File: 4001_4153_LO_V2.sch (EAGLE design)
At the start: 108 parts, among them IC1 74LVC2G17GV,125, IC10 MCP6H01, IC2 74LVC2G17GV,125, IC3 74LVC2G17GV,125, IC4 ADF4001BRUZ, IC5 ATTINY45V-10SU, IC6 7805DT, IC7 7809DT, IC8 LD117ASTR, IC9 ADF4153BRUZ-RL7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

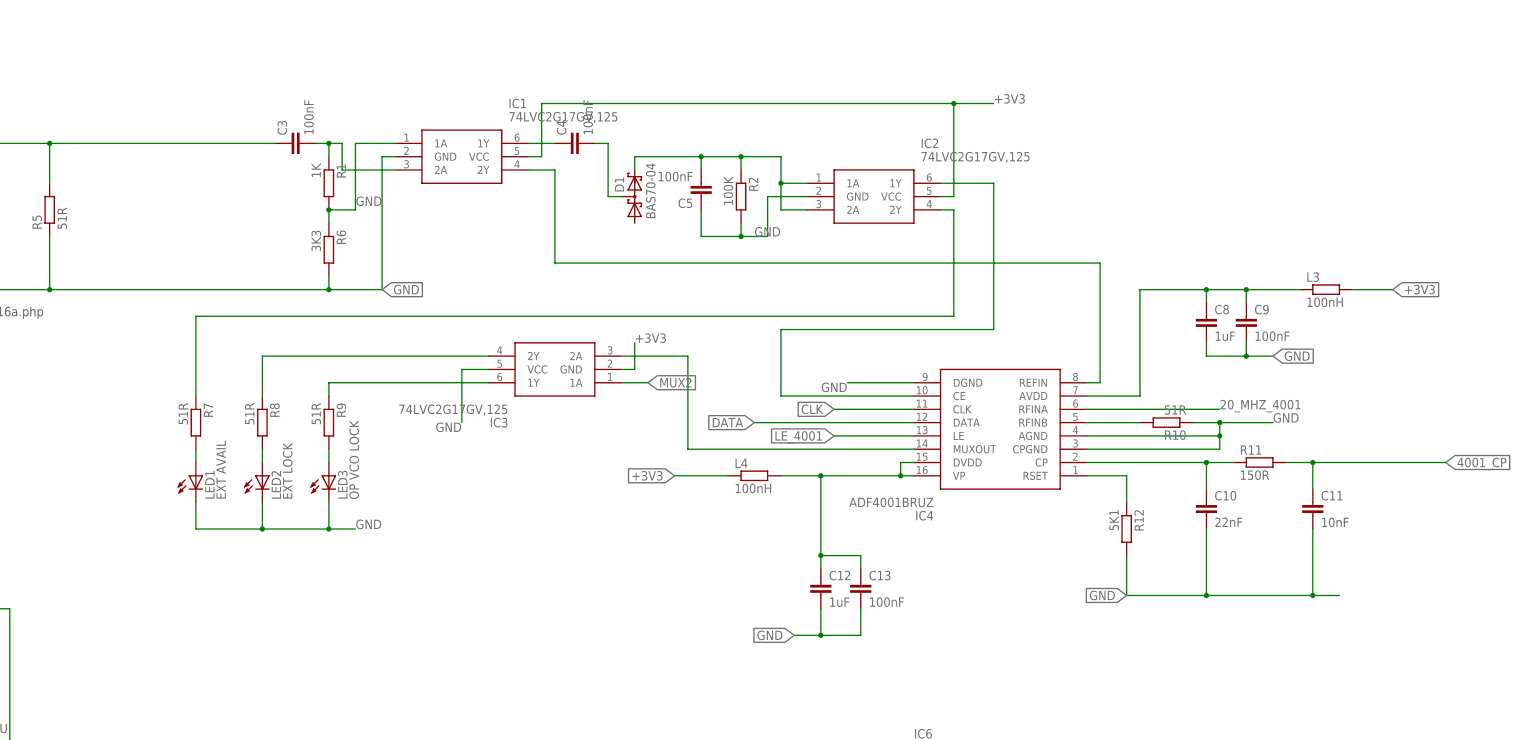
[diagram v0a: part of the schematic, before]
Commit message: Misc circuit revisions
Updated loop filter on 4001, added pullups to MUXOUT
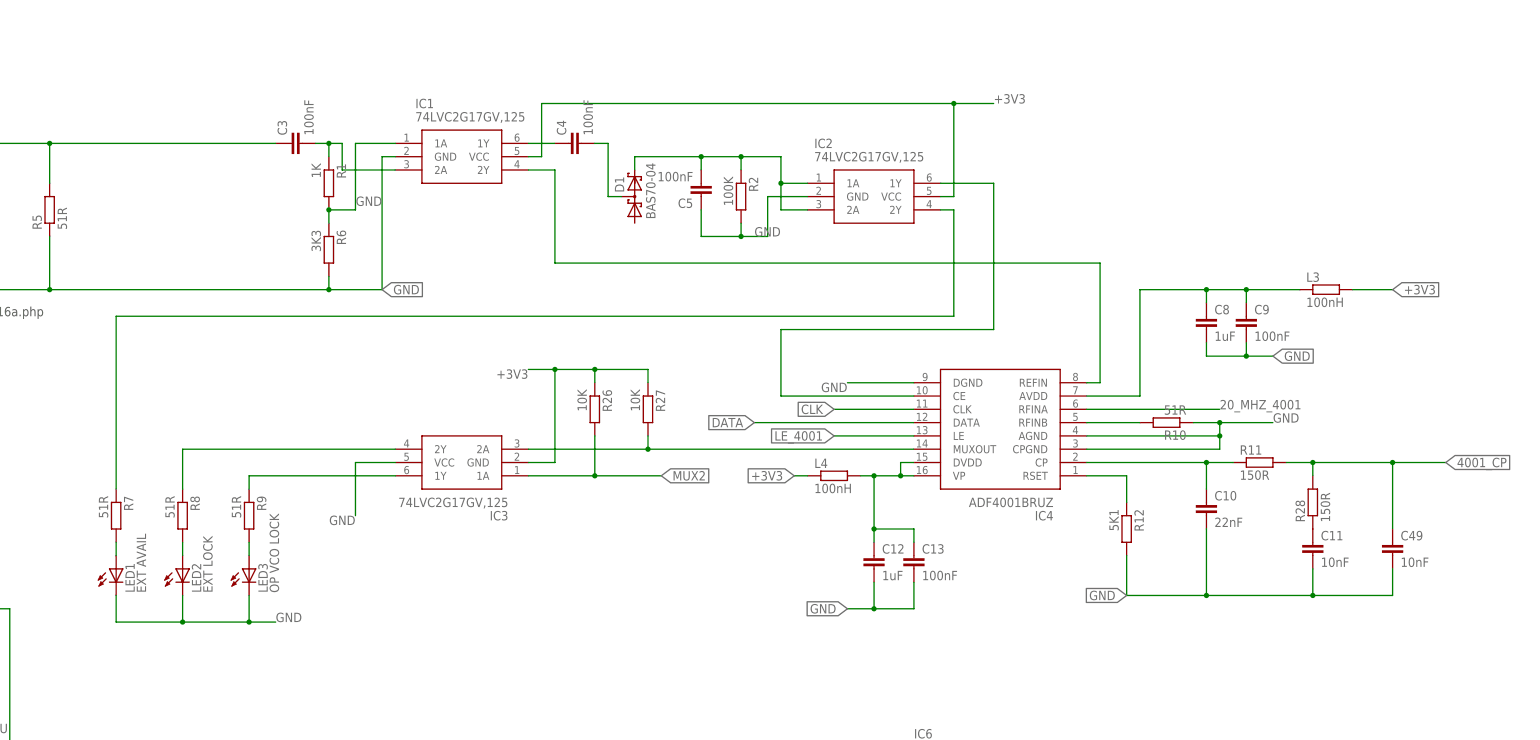
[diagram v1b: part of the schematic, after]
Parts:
- added C49: 10nF, resistor:C-EUC0603
- added R26, R27: 10K, rcl:R-EU_R0603
- added R28: 150R, rcl:R-EU_R0603
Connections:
- new net N$22: C11.1, R28.1
- net +3V3: now also R26.1, R27.1
- net 4001_CP: now also C49.1, R28.2; no longer C11.1
- net GND: now also C49.2
- net MUX2: now also R26.2
- net N$26: now also R27.2
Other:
- moved on the sheet: C11, C12, C13, IC3, L4, LED1, LED2, LED3, R7, R8, R9

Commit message: Output and detector
Moved resistor in output stage to power feed
Swapped C for R in 10MHz detector
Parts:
- removed C4: 100nF, resistor:C-EUC0603
- added R29: 100K, rcl:R-EU_R0603
- IC8: value LD117ASTR -> LD1117AS33TR
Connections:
- net N$11: now also C41.2; no longer R17.2
- net N$12: now also R17.1; no longer L7.1
- net N$21: now also L7.1, R17.2; no longer C41.2, R17.1
- net N$23: now also R29.2; no longer C4.2
- net N$30: now also R29.1; no longer C4.1
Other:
- moved on the sheet: L7, R17
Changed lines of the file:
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@@
 <part name="C21" library="rcl" deviceset="C-EU" device="C0805" value="100nF"/>
 <part name="VR1" library="resistor" deviceset="R-TRIMM" device="4G/J" value="1K"/>
-<part name="IC8" library="v-reg" deviceset="LD117A?*" device="S" technology="TR">
+<part name="IC8" library="v-reg" deviceset="LD117A?*" device="S" technology="TR" value="LD1117AS33TR">
 <attribute name="JLC" value="C108495"/>
 </part>
@@
 <part name="C3" library="resistor" deviceset="C-EU" device="C0603" value="100nF"/>
 <part name="D1" library="diode" deviceset="BAS70-04" device=""/>
-<part name="C4" library="resistor" deviceset="C-EU" device="C0603" value="100nF"/>
 <part name="C5" library="resistor" deviceset="C-EU" device="C0603" value="100nF"/>
 <part name="R2" library="rcl" deviceset="R-EU_" device="R0603" value="100K"/>
@@
 <part name="C49" library="resistor" deviceset="C-EU" device="C0603" value="10nF"/>
 <part name="R28" library="rcl" deviceset="R-EU_" device="R0603" value="150R"/>
+<part name="R29" library="rcl" deviceset="R-EU_" device="R0603" value="100K"/>
 </parts>
 <sheets>
@@
 <instance part="C31" gate="G$1" x="441.96" y="129.54"/>
 <instance part="C30" gate="G$1" x="434.34" y="129.54"/>
-<instance part="L7" gate="G$1" x="457.2" y="121.92" rot="R90"/>
+<instance part="L7" gate="G$1" x="457.2" y="129.54" rot="R90"/>
 <instance part="C38" gate="G$1" x="472.44" y="111.76" rot="R90"/>
 <instance part="R15" gate="G$1" x="403.86" y="114.3" rot="R270"/>
@@
 <instance part="C3" gate="G$1" x="299.72" y="345.44" rot="R90"/>
 <instance part="D1" gate="G$1" x="365.76" y="335.28" rot="R90"/>
-<instance part="C4" gate="G$1" x="353.06" y="345.44" rot="R90"/>
 <instance part="C5" gate="G$1" x="378.46" y="335.28" rot="R180"/>
 <instance part="R2" gate="G$1" x="386.08" y="335.28" rot="R270"/>
@@
 <instance part="C18" gate="G$1" x="454.66" y="223.52"/>
 <instance part="LSP1" gate="1" x="368.3" y="210.82"/>
-<instance part="R17" gate="G$1" x="436.88" y="106.68"/>
+<instance part="R17" gate="G$1" x="457.2" y="116.84" rot="R90"/>
 <instance part="R26" gate="G$1" x="358.14" y="294.64" rot="R270"/>
 <instance part="R27" gate="G$1" x="368.3" y="294.64" rot="R270"/>
 <instance part="C49" gate="G$1" x="510.54" y="269.24"/>
 <instance part="R28" gate="G$1" x="495.3" y="276.86" rot="R90"/>
+<instance part="R29" gate="G$1" x="355.6" y="345.44"/>
 </instances>
 <busses>
@@
 </segment>
 </net>
-<net name="N$11" class="0">
-<segment>
-<pinref part="Q1" gate="G$1" pin="G"/>
-<pinref part="R17" gate="G$1" pin="2"/>
-<wire x1="441.96" y1="106.68" x2="452.12" y2="106.68" width="0.1524" layer="91"/>
-</segment>
-</net>
 <net name="N$12" class="0">
 <segment>
 <pinref part="Q1" gate="G$1" pin="S"/>
 <wire x1="457.2" y1="109.22" x2="457.2" y2="111.76" width="0.1524" layer="91"/>
-<pinref part="L7" gate="G$1" pin="1"/>
 <pinref part="C38" gate="G$1" pin="1"/>
-<wire x1="457.2" y1="111.76" x2="457.2" y2="116.84" width="0.1524" layer="91"/>
 <wire x1="469.9" y1="111.76" x2="457.2" y2="111.76" width="0.1524" layer="91"/>
 <junction x="457.2" y="111.76"/>
+<pinref part="R17" gate="G$1" pin="1"/>
 </segment>
 </net>
@@
 <segment>
 <pinref part="L7" gate="G$1" pin="2"/>
-<wire x1="457.2" y1="127" x2="457.2" y2="137.16" width="0.1524" layer="91"/>
+<wire x1="457.2" y1="134.62" x2="457.2" y2="137.16" width="0.1524" layer="91"/>
 <pinref part="C30" gate="G$1" pin="1"/>
 <wire x1="457.2" y1="137.16" x2="441.96" y2="137.16" width="0.1524" layer="91"/>
@@
 <net name="N$23" class="0">
 <segment>
-<pinref part="C4" gate="G$1" pin="2"/>
-<wire x1="358.14" y1="345.44" x2="360.68" y2="345.44" width="0.1524" layer="91"/>
 <wire x1="360.68" y1="345.44" x2="360.68" y2="335.28" width="0.1524" layer="91"/>
 <pinref part="D1" gate="G$1" pin="C1A2"/>
 <wire x1="360.68" y1="335.28" x2="363.22" y2="335.28" width="0.1524" layer="91"/>
+<pinref part="R29" gate="G$1" pin="2"/>
 </segment>
 </net>
@@
 <segment>
 <pinref part="IC1" gate="G$1" pin="1Y"/>
-<pinref part="C4" gate="G$1" pin="1"/>
 <wire x1="345.44" y1="345.44" x2="350.52" y2="345.44" width="0.1524" layer="91"/>
+<pinref part="R29" gate="G$1" pin="1"/>
 </segment>
 </net>
@@
 </segment>
 </net>
-<net name="N$21" class="0">
-<segment>
-<pinref part="R17" gate="G$1" pin="1"/>
-<wire x1="424.18" y1="106.68" x2="431.8" y2="106.68" width="0.1524" layer="91"/>
-<pinref part="C41" gate="G$1" pin="2"/>
-</segment>
-</net>
 <net name="N$22" class="0">
 <segment>
@@
 </segment>
 </net>
+<net name="N$11" class="0">
+<segment>
+<pinref part="C41" gate="G$1" pin="2"/>
+<pinref part="Q1" gate="G$1" pin="G"/>
+<wire x1="424.18" y1="106.68" x2="452.12" y2="106.68" width="0.1524" layer="91"/>
+</segment>
+</net>
+<net name="N$21" class="0">
+<segment>
+<pinref part="L7" gate="G$1" pin="1"/>
+<wire x1="457.2" y1="121.92" x2="457.2" y2="124.46" width="0.1524" layer="91"/>
+<pinref part="R17" gate="G$1" pin="2"/>
+</segment>
+</net>

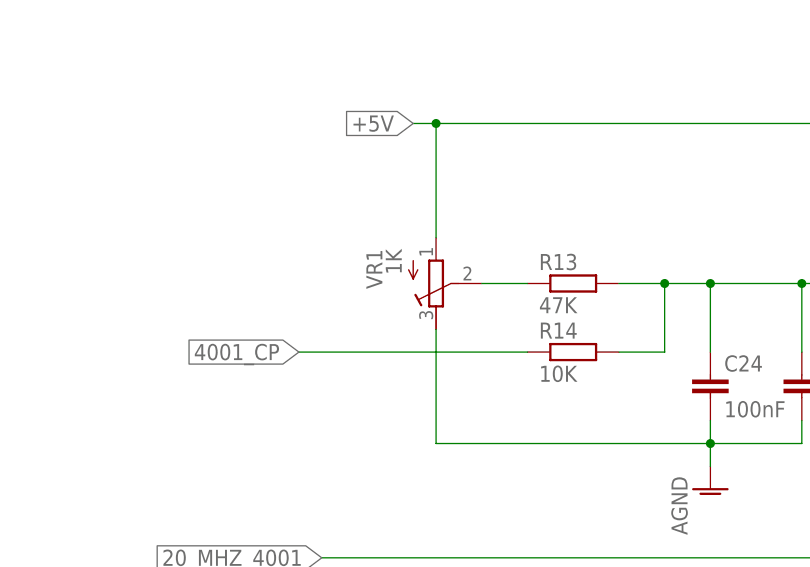
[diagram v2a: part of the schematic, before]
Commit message: multi-turn
replaced single turn pot with multiturn
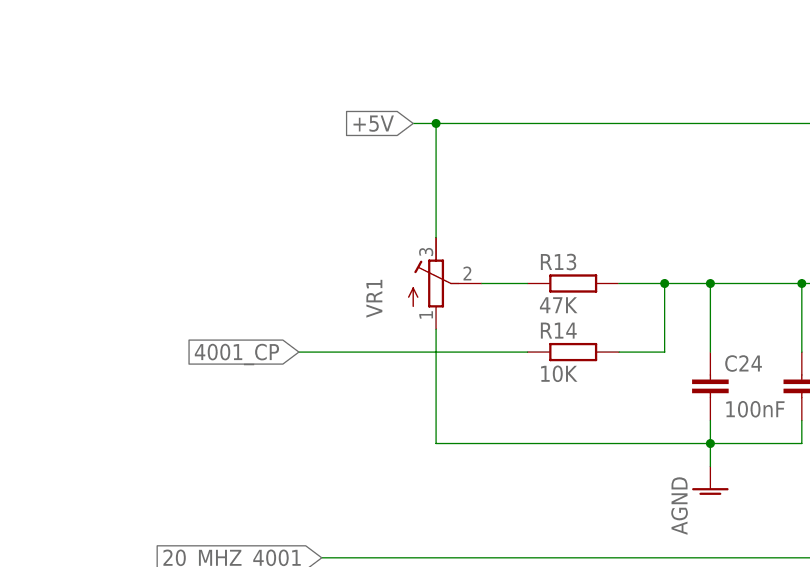
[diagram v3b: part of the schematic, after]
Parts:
- VR1: value 1K -> (none); device resistor:R-TRIMM4G/J -> resistor:R-TRIMM64Y
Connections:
- net +5V: now also VR1.A; no longer VR1.E
- net GND: now also VR1.E; no longer VR1.A
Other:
- moved on the sheet: VR1
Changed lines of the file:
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@@
 <part name="C20" library="rcl" deviceset="C-EU" device="C0805" value="10uF"/>
 <part name="C21" library="rcl" deviceset="C-EU" device="C0805" value="100nF"/>
-<part name="VR1" library="resistor" deviceset="R-TRIMM" device="4G/J" value="1K"/>
 <part name="IC8" library="v-reg" deviceset="LD117A?*" device="S" technology="TR" value="LD1117AS33TR">
 <attribute name="JLC" value="C108495"/>
@@
 <part name="R28" library="rcl" deviceset="R-EU_" device="R0603" value="150R"/>
 <part name="R29" library="rcl" deviceset="R-EU_" device="R0603" value="100K"/>
+<part name="VR1" library="resistor" deviceset="R-TRIMM" device="64Y"/>
 </parts>
 <sheets>
@@
 <instance part="C24" gate="G$1" x="147.32" y="165.1"/>
 <instance part="AGND40" gate="VR1" x="147.32" y="152.4"/>
-<instance part="VR1" gate="G$1" x="116.84" y="175.26" rot="MR180"/>
 <instance part="C36" gate="G$1" x="210.82" y="111.76"/>
 <instance part="C37" gate="G$1" x="218.44" y="111.76"/>
@@
 <instance part="R28" gate="G$1" x="495.3" y="276.86" rot="R90"/>
 <instance part="R29" gate="G$1" x="355.6" y="345.44"/>
+<instance part="VR1" gate="G$1" x="116.84" y="175.26"/>
 </instances>
 <busses>
@@
 <pinref part="C24" gate="G$1" pin="2"/>
 <wire x1="147.32" y1="160.02" x2="147.32" y2="157.48" width="0.1524" layer="91"/>
-<pinref part="VR1" gate="G$1" pin="A"/>
 <wire x1="147.32" y1="157.48" x2="147.32" y2="154.94" width="0.1524" layer="91"/>
 <wire x1="116.84" y1="170.18" x2="116.84" y2="157.48" width="0.1524" layer="91"/>
@@
 <wire x1="147.32" y1="157.48" x2="157.48" y2="157.48" width="0.1524" layer="91"/>
 <wire x1="157.48" y1="157.48" x2="157.48" y2="160.02" width="0.1524" layer="91"/>
+<pinref part="VR1" gate="G$1" pin="E"/>
 </segment>
 <segment>
@@
 <label x="114.3" y="193.04" size="1.778" layer="95" rot="R180" xref="yes"/>
 <wire x1="116.84" y1="193.04" x2="114.3" y2="193.04" width="0.1524" layer="91"/>
-<pinref part="VR1" gate="G$1" pin="E"/>
 <wire x1="116.84" y1="180.34" x2="116.84" y2="193.04" width="0.1524" layer="91"/>
 <junction x="116.84" y="193.04"/>
@@
 <junction x="175.26" y="193.04"/>
 <pinref part="OSC1" gate="G$1" pin="VCC"/>
+<pinref part="VR1" gate="G$1" pin="A"/>
 </segment>
 <segment>
@@
 <net name="N$19" class="0">
 <segment>
-<pinref part="VR1" gate="G$1" pin="S"/>
 <pinref part="R13" gate="G$1" pin="1"/>
 <wire x1="121.92" y1="175.26" x2="127" y2="175.26" width="0.1524" layer="91"/>
-</segment>
-</net>
+<pinref part="VR1" gate="G$1" pin="S"/>
+</segment>
+</net>

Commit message: JLC Release
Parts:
- VR1: value (none) -> 1K0
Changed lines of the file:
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@@
 <part name="R28" library="rcl" deviceset="R-EU_" device="R0603" value="150R"/>
 <part name="R29" library="rcl" deviceset="R-EU_" device="R0603" value="100K"/>
-<part name="VR1" library="resistor" deviceset="R-TRIMM" device="64Y"/>
+<part name="VR1" library="resistor" deviceset="R-TRIMM" device="64Y" value="1K0"/>
 </parts>
 <sheets>

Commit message: JLC release
As issued to JLC
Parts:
- added C4: 100nF, rcl:C-EUC0603
- added IC11: TL431AIDBZR, RF:TL431AIDBZR
- added R30: 470R, rcl:R-EU_R0603
- added R31, R32: 10K, rcl:R-EU_R0603
- IC10: value MCP6H01 -> MCP6H01T-E/LT; MPN (none) -> MCP6H01T-E/LT; OC_FARNELL (none) -> 2920751
- SV1: MPN (none) -> MC-254-06-00-ST-DIP; OC_FARNELL (none) -> 2843525
- VR1: MPN (none) -> 3296Y-1-103LF; OC_FARNELL (none) -> 9353186
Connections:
- new net +5V_PRECISION: C4.1, IC11.CATHODE, R30.2, R32.2, VR1.A
- new net N$42: IC11.CTRL, R31.2, R32.1
- net +12V: now also R30.1
- net +5V: no longer VR1.A
- net GND: now also C4.2, IC11.ANODE, R31.1, TXFMR1.PRI_1, TXFMR1.SEC_3; no longer TXFMR1.PRI_2, TXFMR1.SEC_1
- net N$33: now also TXFMR1.SEC_1; no longer TXFMR1.SEC_3
- net N$34: now also TXFMR1.PRI_2; no longer TXFMR1.PRI_1
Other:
- moved on the sheet: TXFMR1
